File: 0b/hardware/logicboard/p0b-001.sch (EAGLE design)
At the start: 30 parts, among them IC1 7404D, IC4 LTC485S, IC5 LTC485S, J0 DC5V, J7 DIN5, J9 DIN5, X7 NELTRON-7810-XPXC

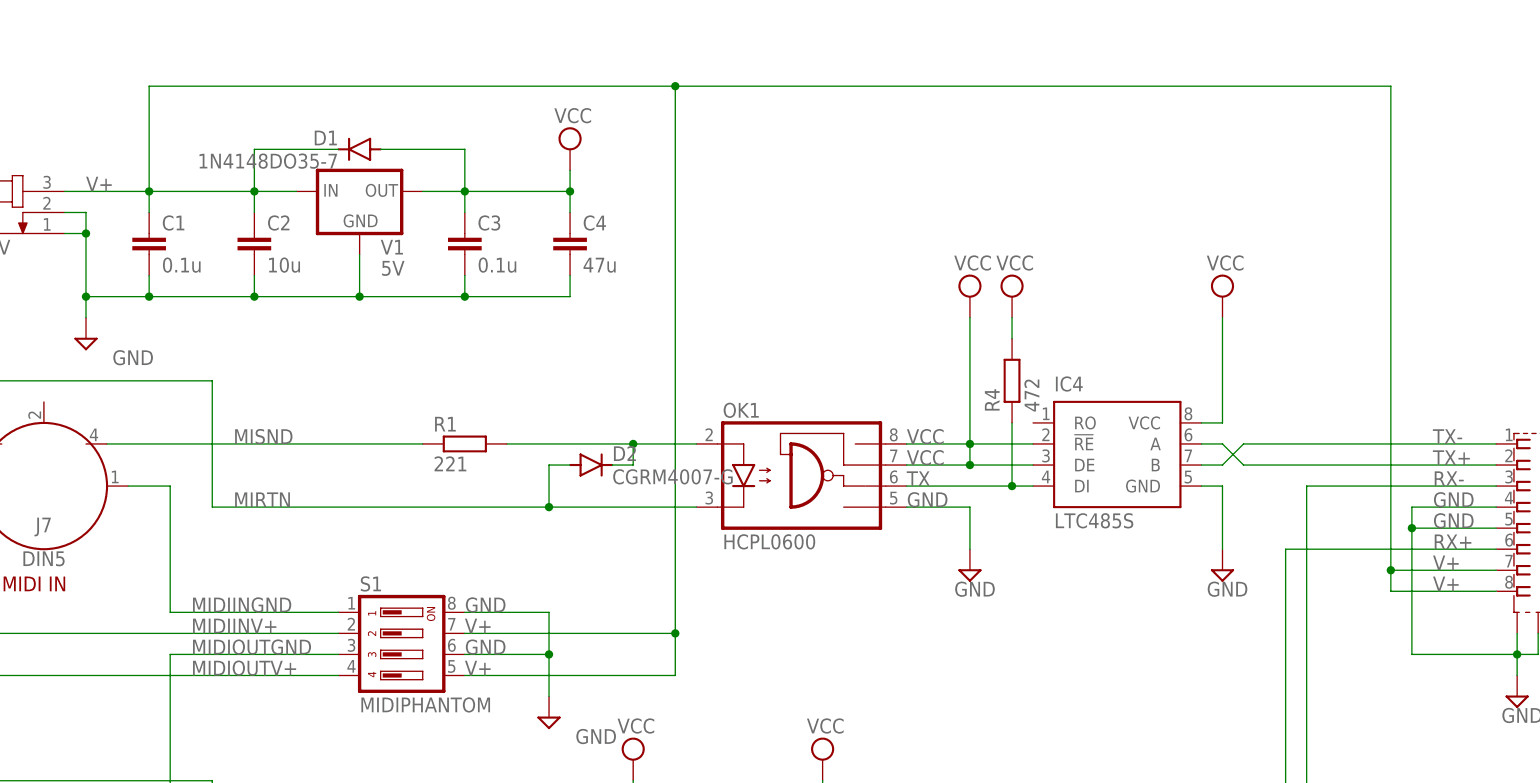
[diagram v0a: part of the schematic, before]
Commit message: Added Direct-5V resistor pattern.
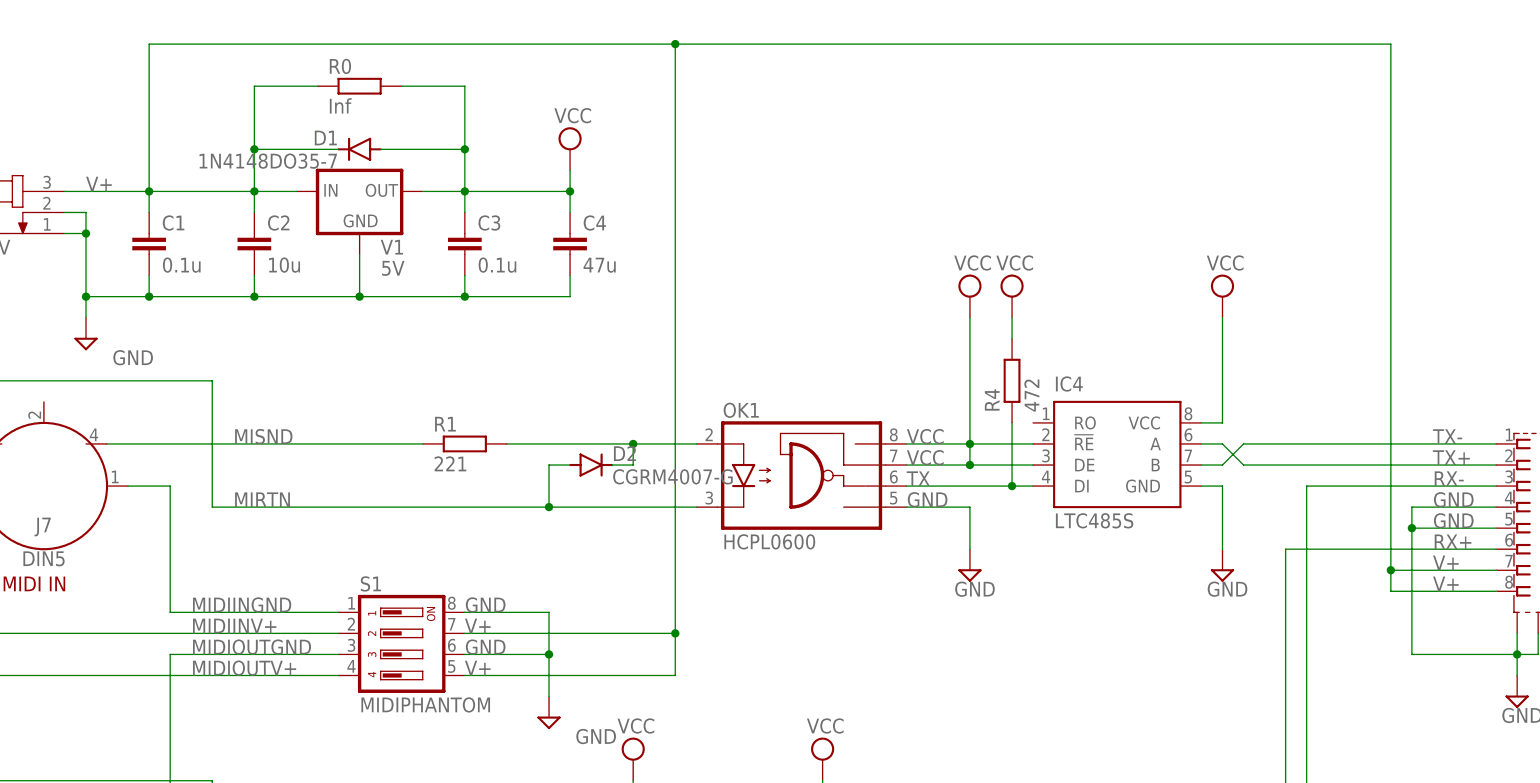
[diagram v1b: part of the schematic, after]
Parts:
- added R0: Inf, rcl:R-EU_M2012
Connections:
- net V+: now also R0.1
- net VCC: now also R0.2
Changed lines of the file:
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@@
 <setting verticaltext="up"/>
 </settings>
-<grid distance="0.1" unitdist="inch" unit="inch" style="lines" multiple="1" display="yes" altdistance="0.01" altunitdist="inch" altunit="inch"/>
+<grid distance="0.1" unitdist="inch" unit="inch" style="lines" multiple="1" display="no" altdistance="0.01" altunitdist="inch" altunit="inch"/>
 <layers>
 <layer number="1" name="Top" color="4" fill="1" visible="no" active="no"/>
@@
 <part name="S1" library="switch-dil" library_urn="urn:adsk.eagle:library:375" deviceset="DIP04YL" device="" package3d_urn="urn:adsk.eagle:package:27255/2" value="MIDIPHANTOM"/>
 <part name="SUPPLY9" library="supply2" library_urn="urn:adsk.eagle:library:372" deviceset="GND" device=""/>
+<part name="R0" library="rcl" library_urn="urn:adsk.eagle:library:334" deviceset="R-EU_" device="M2012" package3d_urn="urn:adsk.eagle:package:23561/2" value="Inf"/>
 </parts>
 <sheets>
@@
 <instance part="SUPPLY9" gate="GND" x="86.36" y="86.36" smashed="yes">
 <attribute name="VALUE" x="89.535" y="83.185" size="1.778" layer="96"/>
+</instance>
+<instance part="R0" gate="G$1" x="63.5" y="162.56" smashed="yes">
+<attribute name="NAME" x="59.69" y="164.0586" size="1.778" layer="95"/>
+<attribute name="VALUE" x="59.69" y="159.258" size="1.778" layer="96"/>
 </instance>
 </instances>
@@
 <wire x1="66.04" y1="154.94" x2="76.2" y2="154.94" width="0.1524" layer="91"/>
 <wire x1="76.2" y1="154.94" x2="76.2" y2="149.86" width="0.1524" layer="91"/>
+<pinref part="R0" gate="G$1" pin="2"/>
+<wire x1="68.58" y1="162.56" x2="76.2" y2="162.56" width="0.1524" layer="91"/>
+<wire x1="76.2" y1="162.56" x2="76.2" y2="154.94" width="0.1524" layer="91"/>
+<junction x="76.2" y="154.94"/>
 </segment>
 </net>
@@
 <pinref part="D1" gate="G$1" pin="C"/>
 <label x="30.48" y="149.86" size="1.778" layer="95"/>
-<wire x1="38.1" y1="149.86" x2="38.1" y2="162.56" width="0.1524" layer="91"/>
+<wire x1="38.1" y1="149.86" x2="38.1" y2="167.64" width="0.1524" layer="91"/>
 <pinref part="X7" gate="G$1" pin="7"/>
 <wire x1="200.66" y1="104.14" x2="187.96" y2="104.14" width="0.1524" layer="91"/>
@@
 <wire x1="187.96" y1="101.6" x2="187.96" y2="104.14" width="0.1524" layer="91"/>
 <junction x="187.96" y="104.14"/>
-<wire x1="38.1" y1="162.56" x2="101.6" y2="162.56" width="0.1524" layer="91"/>
-<wire x1="101.6" y1="162.56" x2="187.96" y2="162.56" width="0.1524" layer="91"/>
-<wire x1="187.96" y1="162.56" x2="187.96" y2="104.14" width="0.1524" layer="91"/>
+<wire x1="38.1" y1="167.64" x2="101.6" y2="167.64" width="0.1524" layer="91"/>
+<wire x1="101.6" y1="167.64" x2="187.96" y2="167.64" width="0.1524" layer="91"/>
+<wire x1="187.96" y1="167.64" x2="187.96" y2="104.14" width="0.1524" layer="91"/>
 <pinref part="S1" gate="1" pin="7"/>
 <wire x1="76.2" y1="96.52" x2="101.6" y2="96.52" width="0.1524" layer="91"/>
@@
 <wire x1="76.2" y1="91.44" x2="101.6" y2="91.44" width="0.1524" layer="91"/>
 <wire x1="101.6" y1="91.44" x2="101.6" y2="96.52" width="0.1524" layer="91"/>
-<wire x1="101.6" y1="96.52" x2="101.6" y2="162.56" width="0.1524" layer="91"/>
+<wire x1="101.6" y1="96.52" x2="101.6" y2="167.64" width="0.1524" layer="91"/>
 <junction x="101.6" y="96.52"/>
-<junction x="101.6" y="162.56"/>
+<junction x="101.6" y="167.64"/>
 <label x="193.04" y="104.14" size="1.778" layer="95"/>
 <label x="193.04" y="101.6" size="1.778" layer="95"/>
 <label x="76.2" y="96.52" size="1.778" layer="95"/>
 <label x="76.2" y="91.44" size="1.778" layer="95"/>
-</segment>
-</net>
+<pinref part="R0" gate="G$1" pin="1"/>
+<wire x1="58.42" y1="162.56" x2="50.8" y2="162.56" width="0.1524" layer="91"/>
+<wire x1="50.8" y1="162.56" x2="50.8" y2="154.94" width="0.1524" layer="91"/>
+<junction x="50.8" y="154.94"/>
+</segment>
+</net>

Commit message: Pinhead.
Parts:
- removed R0: Inf, rcl:R-EU_M2012
- added JP1: (no value), pinhead:PINHD-1X2
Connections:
- net V+: now also JP1.1; no longer R0.1
- net VCC: now also JP1.2; no longer R0.2
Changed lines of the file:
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@@
 <part name="S1" library="switch-dil" library_urn="urn:adsk.eagle:library:375" deviceset="DIP04YL" device="" package3d_urn="urn:adsk.eagle:package:27255/2" value="MIDIPHANTOM"/>
 <part name="SUPPLY9" library="supply2" library_urn="urn:adsk.eagle:library:372" deviceset="GND" device=""/>
-<part name="R0" library="rcl" library_urn="urn:adsk.eagle:library:334" deviceset="R-EU_" device="M2012" package3d_urn="urn:adsk.eagle:package:23561/2" value="Inf"/>
+<part name="JP1" library="pinhead" library_urn="urn:adsk.eagle:library:325" deviceset="PINHD-1X2" device="" package3d_urn="urn:adsk.eagle:package:22435/2"/>
 </parts>
 <sheets>
@@
 <attribute name="VALUE" x="89.535" y="83.185" size="1.778" layer="96"/>
 </instance>
-<instance part="R0" gate="G$1" x="63.5" y="162.56" smashed="yes">
-<attribute name="NAME" x="59.69" y="164.0586" size="1.778" layer="95"/>
-<attribute name="VALUE" x="59.69" y="159.258" size="1.778" layer="96"/>
+<instance part="JP1" gate="G$1" x="63.5" y="165.1" smashed="yes" rot="R90">
+<attribute name="NAME" x="57.785" y="158.75" size="1.778" layer="95" rot="R90"/>
+<attribute name="VALUE" x="68.58" y="158.75" size="1.778" layer="96" rot="R90"/>
 </instance>
 </instances>
@@
 <wire x1="66.04" y1="154.94" x2="76.2" y2="154.94" width="0.1524" layer="91"/>
 <wire x1="76.2" y1="154.94" x2="76.2" y2="149.86" width="0.1524" layer="91"/>
-<pinref part="R0" gate="G$1" pin="2"/>
-<wire x1="68.58" y1="162.56" x2="76.2" y2="162.56" width="0.1524" layer="91"/>
-<wire x1="76.2" y1="162.56" x2="76.2" y2="154.94" width="0.1524" layer="91"/>
+<wire x1="63.5" y1="160.02" x2="76.2" y2="160.02" width="0.1524" layer="91"/>
+<wire x1="76.2" y1="160.02" x2="76.2" y2="154.94" width="0.1524" layer="91"/>
 <junction x="76.2" y="154.94"/>
+<pinref part="JP1" gate="G$1" pin="2"/>
+<wire x1="63.5" y1="162.56" x2="63.5" y2="160.02" width="0.1524" layer="91"/>
 </segment>
 </net>
@@
 <label x="76.2" y="96.52" size="1.778" layer="95"/>
 <label x="76.2" y="91.44" size="1.778" layer="95"/>
-<pinref part="R0" gate="G$1" pin="1"/>
-<wire x1="58.42" y1="162.56" x2="50.8" y2="162.56" width="0.1524" layer="91"/>
-<wire x1="50.8" y1="162.56" x2="50.8" y2="154.94" width="0.1524" layer="91"/>
+<wire x1="60.96" y1="160.02" x2="50.8" y2="160.02" width="0.1524" layer="91"/>
+<wire x1="50.8" y1="160.02" x2="50.8" y2="154.94" width="0.1524" layer="91"/>
 <junction x="50.8" y="154.94"/>
-</segment>
-</net>
+<pinref part="JP1" gate="G$1" pin="1"/>
+<wire x1="60.96" y1="162.56" x2="60.96" y2="160.02" width="0.1524" layer="91"/>
+</segment>
+</net>

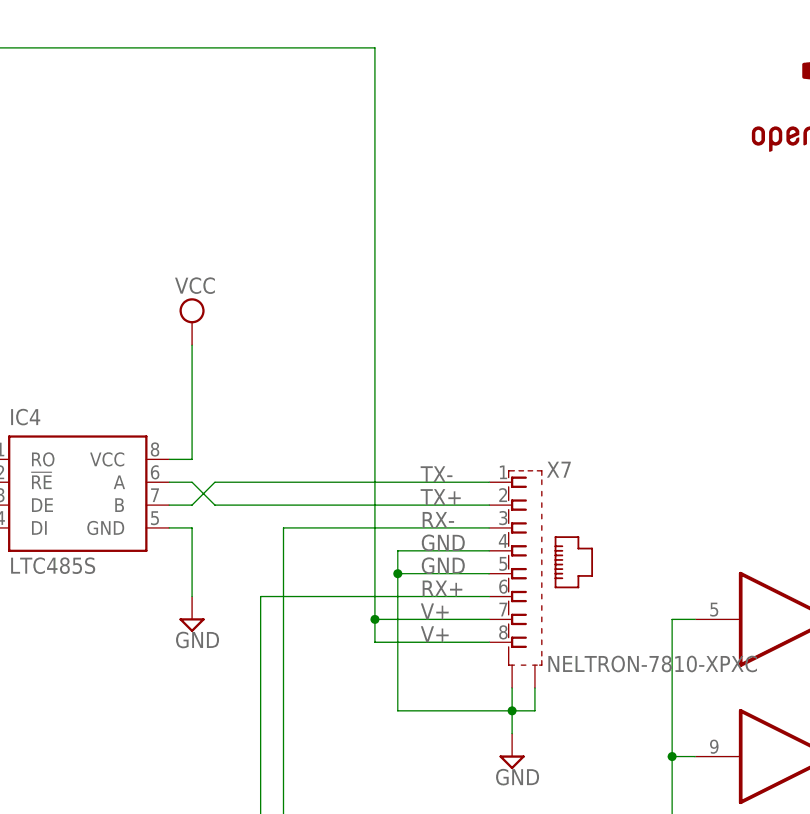
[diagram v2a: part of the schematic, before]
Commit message: Added PoE R.
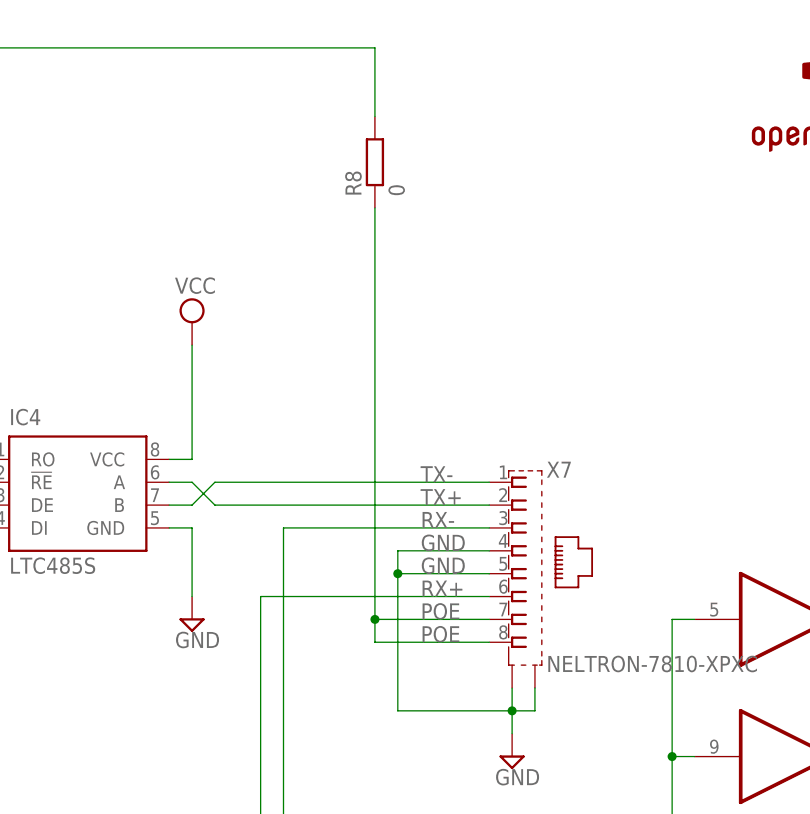
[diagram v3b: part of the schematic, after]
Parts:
- added R8: 0, rcl:R-EU_M2012
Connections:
- new net POE: R8.1, X7.7, X7.8
- net V+: now also R8.2; no longer X7.7, X7.8
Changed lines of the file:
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@@
 <part name="SUPPLY9" library="supply2" library_urn="urn:adsk.eagle:library:372" deviceset="GND" device=""/>
 <part name="JP1" library="pinhead" library_urn="urn:adsk.eagle:library:325" deviceset="PINHD-1X2" device="" package3d_urn="urn:adsk.eagle:package:22435/2"/>
+<part name="R8" library="rcl" library_urn="urn:adsk.eagle:library:334" deviceset="R-EU_" device="M2012" package3d_urn="urn:adsk.eagle:package:23561/2" value="0"/>
 </parts>
 <sheets>
@@
 <attribute name="NAME" x="57.785" y="158.75" size="1.778" layer="95" rot="R90"/>
 <attribute name="VALUE" x="68.58" y="158.75" size="1.778" layer="96" rot="R90"/>
+</instance>
+<instance part="R8" gate="G$1" x="187.96" y="154.94" smashed="yes" rot="R90">
+<attribute name="NAME" x="186.4614" y="151.13" size="1.778" layer="95" rot="R90"/>
+<attribute name="VALUE" x="191.262" y="151.13" size="1.778" layer="96" rot="R90"/>
 </instance>
 </instances>
@@
 <label x="30.48" y="149.86" size="1.778" layer="95"/>
 <wire x1="38.1" y1="149.86" x2="38.1" y2="167.64" width="0.1524" layer="91"/>
-<pinref part="X7" gate="G$1" pin="7"/>
-<wire x1="200.66" y1="104.14" x2="187.96" y2="104.14" width="0.1524" layer="91"/>
-<pinref part="X7" gate="G$1" pin="8"/>
-<wire x1="200.66" y1="101.6" x2="187.96" y2="101.6" width="0.1524" layer="91"/>
-<wire x1="187.96" y1="101.6" x2="187.96" y2="104.14" width="0.1524" layer="91"/>
-<junction x="187.96" y="104.14"/>
 <wire x1="38.1" y1="167.64" x2="101.6" y2="167.64" width="0.1524" layer="91"/>
 <wire x1="101.6" y1="167.64" x2="187.96" y2="167.64" width="0.1524" layer="91"/>
-<wire x1="187.96" y1="167.64" x2="187.96" y2="104.14" width="0.1524" layer="91"/>
 <pinref part="S1" gate="1" pin="7"/>
 <wire x1="76.2" y1="96.52" x2="101.6" y2="96.52" width="0.1524" layer="91"/>
@@
 <junction x="101.6" y="96.52"/>
 <junction x="101.6" y="167.64"/>
-<label x="193.04" y="104.14" size="1.778" layer="95"/>
-<label x="193.04" y="101.6" size="1.778" layer="95"/>
 <label x="76.2" y="96.52" size="1.778" layer="95"/>
 <label x="76.2" y="91.44" size="1.778" layer="95"/>
@@
 <pinref part="JP1" gate="G$1" pin="1"/>
 <wire x1="60.96" y1="162.56" x2="60.96" y2="160.02" width="0.1524" layer="91"/>
+<pinref part="R8" gate="G$1" pin="2"/>
+<wire x1="187.96" y1="167.64" x2="187.96" y2="160.02" width="0.1524" layer="91"/>
 </segment>
 </net>
@@
 </segment>
 </net>
+<net name="POE" class="1">
+<segment>
+<pinref part="X7" gate="G$1" pin="7"/>
+<wire x1="200.66" y1="104.14" x2="187.96" y2="104.14" width="0.1524" layer="91"/>
+<pinref part="X7" gate="G$1" pin="8"/>
+<wire x1="200.66" y1="101.6" x2="187.96" y2="101.6" width="0.1524" layer="91"/>
+<wire x1="187.96" y1="101.6" x2="187.96" y2="104.14" width="0.1524" layer="91"/>
+<label x="193.04" y="104.14" size="1.778" layer="95"/>
+<label x="193.04" y="101.6" size="1.778" layer="95"/>
+<wire x1="187.96" y1="149.86" x2="187.96" y2="104.14" width="0.1524" layer="91"/>
+<junction x="187.96" y="104.14"/>
+<pinref part="R8" gate="G$1" pin="1"/>
+</segment>
+</net>

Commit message: Pinhead.
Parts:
- added JP2: (no value), pinhead:PINHD-1X2
- R8: value 0 -> 20
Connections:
- new net POERAW: JP2.1, R8.1
- net POE: now also JP2.2; no longer R8.1
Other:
- note added: "TYPE B"
- moved on the sheet: IC1A, IC1B, R2, R3, R4, R5, R8

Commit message: Xbar.
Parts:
- added JMP1, JMP2, JMP3, JMP4: 0R-JUMPA, jump-0r-smd:0R-JUMPA
- JP1, JP2: device pinhead:PINHD-1X2 -> jumper:JP1E
- R7: value 220 -> 102
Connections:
- new net RX+/TX+: JMP4-0R.2, X7.6
- new net RX-/TX-: JMP3-0R.2, X7.3
- new net TX+/RX+: JMP2-0R.2, X7.2
- new net TX-/RX-: JMP1-0R.2, X7.1
- net RX+: now also JMP2-0R.3, JMP4-0R.1, R6.1; no longer R6.2, X7.6
- net RX-: now also JMP1-0R.3, JMP3-0R.1, R6.2; no longer R6.1, X7.3
- net TX+: now also JMP2-0R.1, JMP4-0R.3; no longer X7.2
- net TX-: now also JMP1-0R.1, JMP3-0R.3; no longer X7.1
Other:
- note removed: "TYPE B"
- moved on the sheet: IC1C, IC1D, IC1E, IC1F, R6
